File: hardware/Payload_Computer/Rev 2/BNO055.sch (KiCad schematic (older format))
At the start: 1 part, among them U501 BNO055

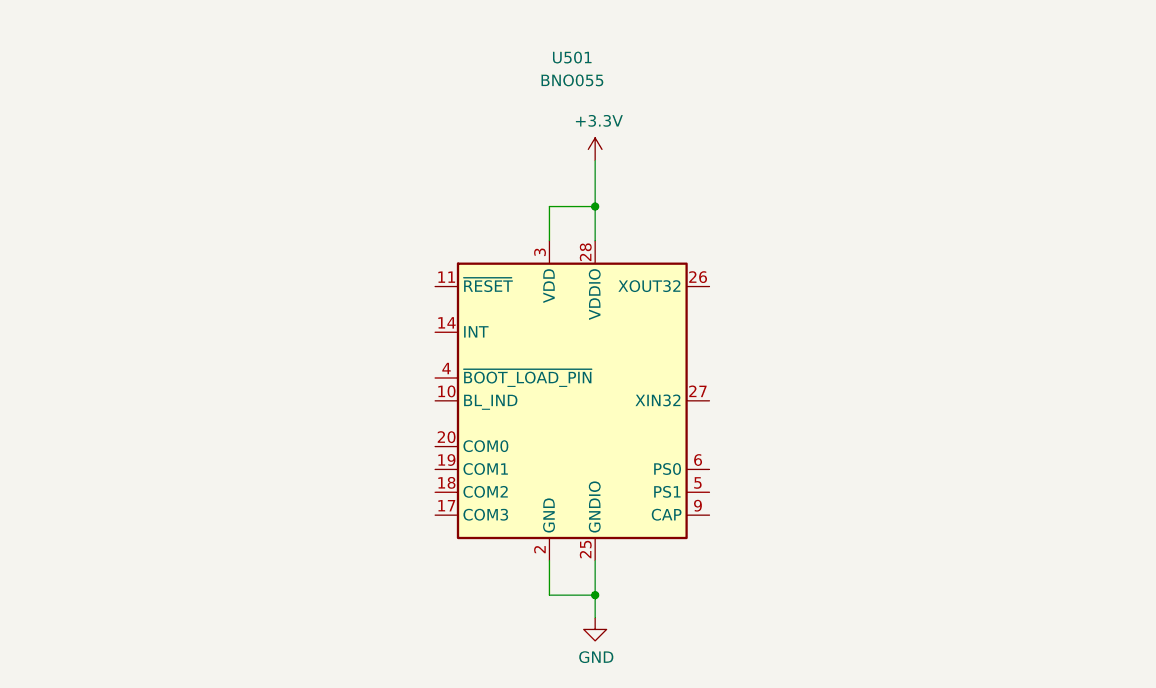
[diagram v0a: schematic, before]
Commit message: Added SD card reader
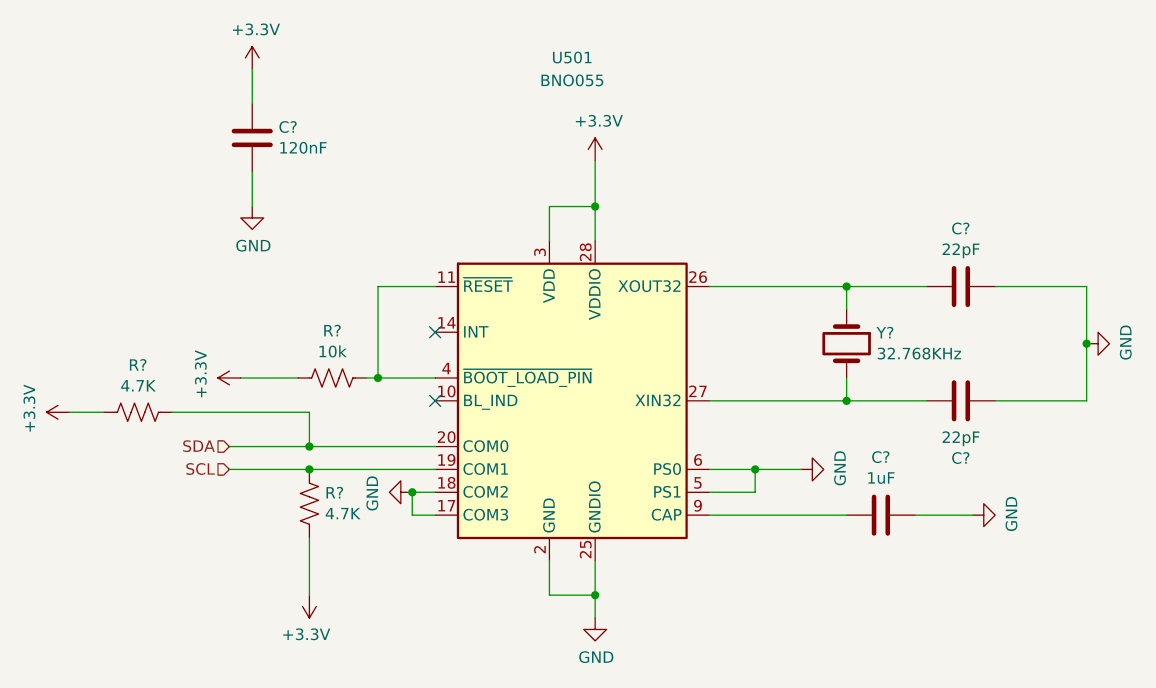
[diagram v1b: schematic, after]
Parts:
- added C? (x2): 22pF, symbol Device:C
- added C?: 120nF, symbol Device:C
- added C?: 1uF, symbol Device:C
- added R?: 10k, symbol Device:R_US
- added R? (x2): 4.7K, symbol Device:R_US
- added Y?: 32.768KHz, symbol Device:Crystal
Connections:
- net +3V3: now also C?.1, R?.1, R?.1, R?.2
- net GND: now also U501.17 (COM3), U501.18 (COM2), U501.5 (PS1), U501.6 (PS0), C?.1, C?.2, C?.2, C?.2
- net at U501.11 (~RESET): now also U501.4 (~BOOT_LOAD_PIN), R?.2
- net SCL: now reaches U501.19 (COM1)
- net SCL: now also R?.1
- net SDA: now reaches U501.20 (COM0)
- net SDA: now also R?.2
- net at U501.26 (XOUT32): now also C?.2, Y?.1
- net at U501.27 (XIN32): now also C?.1, Y?.2
- net at U501.9 (CAP): now also C?.1
- no-connect marks 0 -> 2

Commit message: Did some stuff
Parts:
- gave numbers to parts that had none: 8
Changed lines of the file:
@@
 $Descr A4 11693 8268
 encoding utf-8
-Sheet 5 6
+Sheet 5 7
 Title ""
 Date ""
@@
 	6350 4450 6350 4550
 $Comp
-L Device:Crystal Y?
+L Device:Crystal Y501
 U 1 1 60694DEB
 P 7450 3350
-F 0 "Y?" V 7404 3481 50  0000 L CNN
+F 0 "Y501" V 7404 3481 50  0000 L CNN
 F 1 "32.768KHz" V 7495 3481 50  0000 L CNN
 F 2 "" H 7450 3350 50  0001 C CNN
@@
 	7450 3100 7450 3200
 $Comp
-L Device:C C?
+L Device:C C504
 U 1 1 606960B2
 P 7950 3600
-F 0 "C?" V 7698 3600 50  0000 C CNN
+F 0 "C504" V 7698 3600 50  0000 C CNN
 F 1 "22pF" V 7789 3600 50  0000 C CNN
 F 2 "" H 7988 3450 50  0001 C CNN
@@
 	7450 3500 7450 3600
 $Comp
-L power:GND #PWR?
+L power:GND #PWR0511
 U 1 1 60697238
 P 8500 3350
-F 0 "#PWR?" H 8500 3100 50  0001 C CNN
+F 0 "#PWR0511" H 8500 3100 50  0001 C CNN
 F 1 "GND" H 8505 3177 50  0000 C CNN
 F 2 "" H 8500 3350 50  0001 C CNN
@@
 Connection ~ 8500 3350
 $Comp
-L Device:C C?
+L Device:C C501
 U 1 1 606981BA
 P 4850 2450
-F 0 "C?" H 4965 2496 50  0000 L CNN
+F 0 "C501" H 4965 2496 50  0000 L CNN
 F 1 "120nF" H 4965 2405 50  0000 L CNN
 F 2 "" H 4888 2300 50  0001 C CNN
@@
 $EndComp
 $Comp
-L power:+3.3V #PWR?
+L power:+3.3V #PWR0505
 U 1 1 60698CC9
 P 4850 2150
-F 0 "#PWR?" H 4850 2000 50  0001 C CNN
+F 0 "#PWR0505" H 4850 2000 50  0001 C CNN
 F 1 "+3.3V" H 4865 2323 50  0000 C CNN
 F 2 "" H 4850 2150 50  0001 C CNN
@@
 $EndComp
 $Comp
-L power:GND #PWR?
+L power:GND #PWR0506
 U 1 1 606990FD
 P 4850 2750
-F 0 "#PWR?" H 4850 2500 50  0001 C CNN
+F 0 "#PWR0506" H 4850 2500 50  0001 C CNN
 F 1 "GND" H 4855 2577 50  0000 C CNN
 F 2 "" H 4850 2750 50  0001 C CNN
@@
 	4850 2600 4850 2750
 $Comp
-L Device:R_US R?
+L Device:R_US R503
 U 1 1 60699D24
 P 5200 3500
-F 0 "R?" V 5405 3500 50  0000 C CNN
+F 0 "R503" V 5405 3500 50  0000 C CNN
 F 1 "10k" V 5314 3500 50  0000 C CNN
 F 2 "" V 5240 3490 50  0001 C CNN
@@
 	5650 3500 5400 3500
 $Comp
-L power:+3.3V #PWR?
+L power:+3.3V #PWR0504
 U 1 1 6069AD75
 P 4800 3500
-F 0 "#PWR?" H 4800 3350 50  0001 C CNN
+F 0 "#PWR0504" H 4800 3350 50  0001 C CNN
 F 1 "+3.3V" H 4815 3673 50  0000 C CNN
 F 2 "" H 4800 3500 50  0001 C CNN
@@
 	5050 3500 4800 3500
 $Comp
-L power:GND #PWR?
+L power:GND #PWR0509
 U 1 1 6069B85A
 P 7250 3900
-F 0 "#PWR?" H 7250 3650 50  0001 C CNN
+F 0 "#PWR0509" H 7250 3650 50  0001 C CNN
 F 1 "GND" H 7255 3727 50  0000 C CNN
 F 2 "" H 7250 3900 50  0001 C CNN
@@
 	7050 3900 7250 3900
 $Comp
-L Device:C C?
+L Device:C C502
 U 1 1 6069C4D9
 P 7600 4100
-F 0 "C?" V 7852 4100 50  0000 C CNN
+F 0 "C502" V 7852 4100 50  0000 C CNN
 F 1 "1uF" V 7761 4100 50  0000 C CNN
 F 2 "" H 7638 3950 50  0001 C CNN
@@
 	6850 4100 7450 4100
 $Comp
-L power:GND #PWR?
+L power:GND #PWR0510
 U 1 1 6069D4D9
 P 8000 4100
-F 0 "#PWR?" H 8000 3850 50  0001 C CNN
+F 0 "#PWR0510" H 8000 3850 50  0001 C CNN
 F 1 "GND" H 8005 3927 50  0000 C CNN
 F 2 "" H 8000 4100 50  0001 C CNN
@@
 	4750 3900 5100 3900
 $Comp
-L Device:R_US R?
+L Device:R_US R502
 U 1 1 6069F9B0
 P 5100 4050
-F 0 "R?" H 5168 4096 50  0000 L CNN
+F 0 "R502" H 5168 4096 50  0000 L CNN
 F 1 "4.7K" H 5168 4005 50  0000 L CNN
 F 2 "" V 5140 4040 50  0001 C CNN
@@
 	5100 3900 5650 3900
 $Comp
-L power:+3.3V #PWR?
+L power:+3.3V #PWR0507
 U 1 1 606A0192
 P 5100 4450
-F 0 "#PWR?" H 5100 4300 50  0001 C CNN
+F 0 "#PWR0507" H 5100 4300 50  0001 C CNN
 F 1 "+3.3V" H 5115 4623 50  0000 C CNN
 F 2 "" H 5100 4450 50  0001 C CNN
@@
 	5100 4200 5100 4450
 $Comp
-L Device:R_US R?
+L Device:R_US R501
 U 1 1 606A0E24
 P 4350 3650
-F 0 "R?" V 4555 3650 50  0000 C CNN
+F 0 "R501" V 4555 3650 50  0000 C CNN
 F 1 "4.7K" V 4464 3650 50  0000 C CNN
 F 2 "" V 4390 3640 50  0001 C CNN
@@
 	5100 3800 4750 3800
 $Comp
-L power:+3.3V #PWR?
+L power:+3.3V #PWR0503
 U 1 1 606A2268
 P 4050 3650
-F 0 "#PWR?" H 4050 3500 50  0001 C CNN
+F 0 "#PWR0503" H 4050 3500 50  0001 C CNN
 F 1 "+3.3V" H 4065 3823 50  0000 C CNN
 F 2 "" H 4050 3650 50  0001 C CNN
@@
 	4200 3650 4050 3650
 $Comp
-L power:GND #PWR?
+L power:GND #PWR0508
 U 1 1 606A3093
 P 5550 4000
-F 0 "#PWR?" H 5550 3750 50  0001 C CNN
+F 0 "#PWR0508" H 5550 3750 50  0001 C CNN
 F 1 "GND" H 5555 3827 50  0000 C CNN
 F 2 "" H 5550 4000 50  0001 C CNN
@@
 	5650 4000 5550 4000
 $Comp
-L Device:C C?
+L Device:C C503
 U 1 1 606A4E8A
 P 7950 3100
-F 0 "C?" V 7698 3100 50  0000 C CNN
+F 0 "C503" V 7698 3100 50  0000 C CNN
 F 1 "22pF" V 7789 3100 50  0000 C CNN
 F 2 "" H 7988 2950 50  0001 C CNN

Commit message: Finished some routing
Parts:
- removed R501, R502: 4.7K, symbol Device:R_US
- C501, C502, C503, C504: footprint (none) -> Capacitor_SMD:C_0603_1608Metric_Pad1.08x0.95mm_HandSolder
- R503: footprint (none) -> Resistor_SMD:R_0603_1608Metric_Pad0.98x0.95mm_HandSolder
- Y501: footprint (none) -> footprints:crystal; Digikey (none) -> 887-1425-1-ND
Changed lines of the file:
@@
 F 0 "Y501" V 7404 3481 50  0000 L CNN
 F 1 "32.768KHz" V 7495 3481 50  0000 L CNN
-F 2 "" H 7450 3350 50  0001 C CNN
+F 2 "footprints:crystal" H 7450 3350 50  0001 C CNN
 F 3 "~" H 7450 3350 50  0001 C CNN
+F 4 "887-1425-1-ND" V 7450 3350 50  0001 C CNN "Digikey"
 	1    7450 3350
 	0    1    1    0
@@
 F 0 "C504" V 7698 3600 50  0000 C CNN
 F 1 "22pF" V 7789 3600 50  0000 C CNN
-F 2 "" H 7988 3450 50  0001 C CNN
+F 2 "Capacitor_SMD:C_0603_1608Metric_Pad1.08x0.95mm_HandSolder" H 7988 3450 50  0001 C CNN
 F 3 "~" H 7950 3600 50  0001 C CNN
 	1    7950 3600
@@
 F 0 "C501" H 4965 2496 50  0000 L CNN
 F 1 "120nF" H 4965 2405 50  0000 L CNN
-F 2 "" H 4888 2300 50  0001 C CNN
+F 2 "Capacitor_SMD:C_0603_1608Metric_Pad1.08x0.95mm_HandSolder" H 4888 2300 50  0001 C CNN
 F 3 "~" H 4850 2450 50  0001 C CNN
 	1    4850 2450
@@
 F 0 "R503" V 5405 3500 50  0000 C CNN
 F 1 "10k" V 5314 3500 50  0000 C CNN
-F 2 "" V 5240 3490 50  0001 C CNN
+F 2 "Resistor_SMD:R_0603_1608Metric_Pad0.98x0.95mm_HandSolder" V 5240 3490 50  0001 C CNN
 F 3 "~" H 5200 3500 50  0001 C CNN
 	1    5200 3500
@@
 F 0 "C502" V 7852 4100 50  0000 C CNN
 F 1 "1uF" V 7761 4100 50  0000 C CNN
-F 2 "" H 7638 3950 50  0001 C CNN
+F 2 "Capacitor_SMD:C_0603_1608Metric_Pad1.08x0.95mm_HandSolder" H 7638 3950 50  0001 C CNN
 F 3 "~" H 7600 4100 50  0001 C CNN
 	1    7600 4100
@@
 Text HLabel 4750 3800 0    50   Input ~ 0
 SDA
-Wire Wire Line
-	5650 3800 5100 3800
-Wire Wire Line
-	4750 3900 5100 3900
-$Comp
-L Device:R_US R502
-U 1 1 6069F9B0
-P 5100 4050
-F 0 "R502" H 5168 4096 50  0000 L CNN
-F 1 "4.7K" H 5168 4005 50  0000 L CNN
-F 2 "" V 5140 4040 50  0001 C CNN
-F 3 "~" H 5100 4050 50  0001 C CNN
-	1    5100 4050
-	1    0    0    -1
-$EndComp
-Connection ~ 5100 3900
-Wire Wire Line
-	5100 3900 5650 3900
-$Comp
-L power:+3.3V #PWR0507
-U 1 1 606A0192
-P 5100 4450
-F 0 "#PWR0507" H 5100 4300 50  0001 C CNN
-F 1 "+3.3V" H 5115 4623 50  0000 C CNN
-F 2 "" H 5100 4450 50  0001 C CNN
-F 3 "" H 5100 4450 50  0001 C CNN
-	1    5100 4450
-	-1   0    0    1
-$EndComp
-Wire Wire Line
-	5100 4200 5100 4450
-$Comp
-L Device:R_US R501
-U 1 1 606A0E24
-P 4350 3650
-F 0 "R501" V 4555 3650 50  0000 C CNN
-F 1 "4.7K" V 4464 3650 50  0000 C CNN
-F 2 "" V 4390 3640 50  0001 C CNN
-F 3 "~" H 4350 3650 50  0001 C CNN
-	1    4350 3650
-	0    -1   -1   0
-$EndComp
-Wire Wire Line
-	5100 3800 5100 3650
-Wire Wire Line
-	5100 3650 4500 3650
-Connection ~ 5100 3800
-Wire Wire Line
-	5100 3800 4750 3800
-$Comp
-L power:+3.3V #PWR0503
-U 1 1 606A2268
-P 4050 3650
-F 0 "#PWR0503" H 4050 3500 50  0001 C CNN
-F 1 "+3.3V" H 4065 3823 50  0000 C CNN
-F 2 "" H 4050 3650 50  0001 C CNN
-F 3 "" H 4050 3650 50  0001 C CNN
-	1    4050 3650
-	0    -1   -1   0
-$EndComp
-Wire Wire Line
-	4200 3650 4050 3650
 $Comp
 L power:GND #PWR0508
@@
 F 0 "C503" V 7698 3100 50  0000 C CNN
 F 1 "22pF" V 7789 3100 50  0000 C CNN
-F 2 "" H 7988 2950 50  0001 C CNN
+F 2 "Capacitor_SMD:C_0603_1608Metric_Pad1.08x0.95mm_HandSolder" H 7988 2950 50  0001 C CNN
 F 3 "~" H 7950 3100 50  0001 C CNN
 	1    7950 3100
@@
 NoConn ~ 5650 3600
 NoConn ~ 5650 3300
+Wire Wire Line
+	4750 3900 5650 3900
+Wire Wire Line
+	4750 3800 5650 3800
 $EndSCHEMATC
